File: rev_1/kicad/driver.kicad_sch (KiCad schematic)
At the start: 85 parts, among them Q1 IRFZ44NPBF, Q2 IRFZ44NPBF, Q3 IRFZ44NPBF, Q4 IRFZ44NPBF, Q5 IRFZ44NPBF, Q6 IRFZ44NPBF, U1 ir2104, U2 ir2104, U3 ir2104, U4 INA180A2IDBVR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

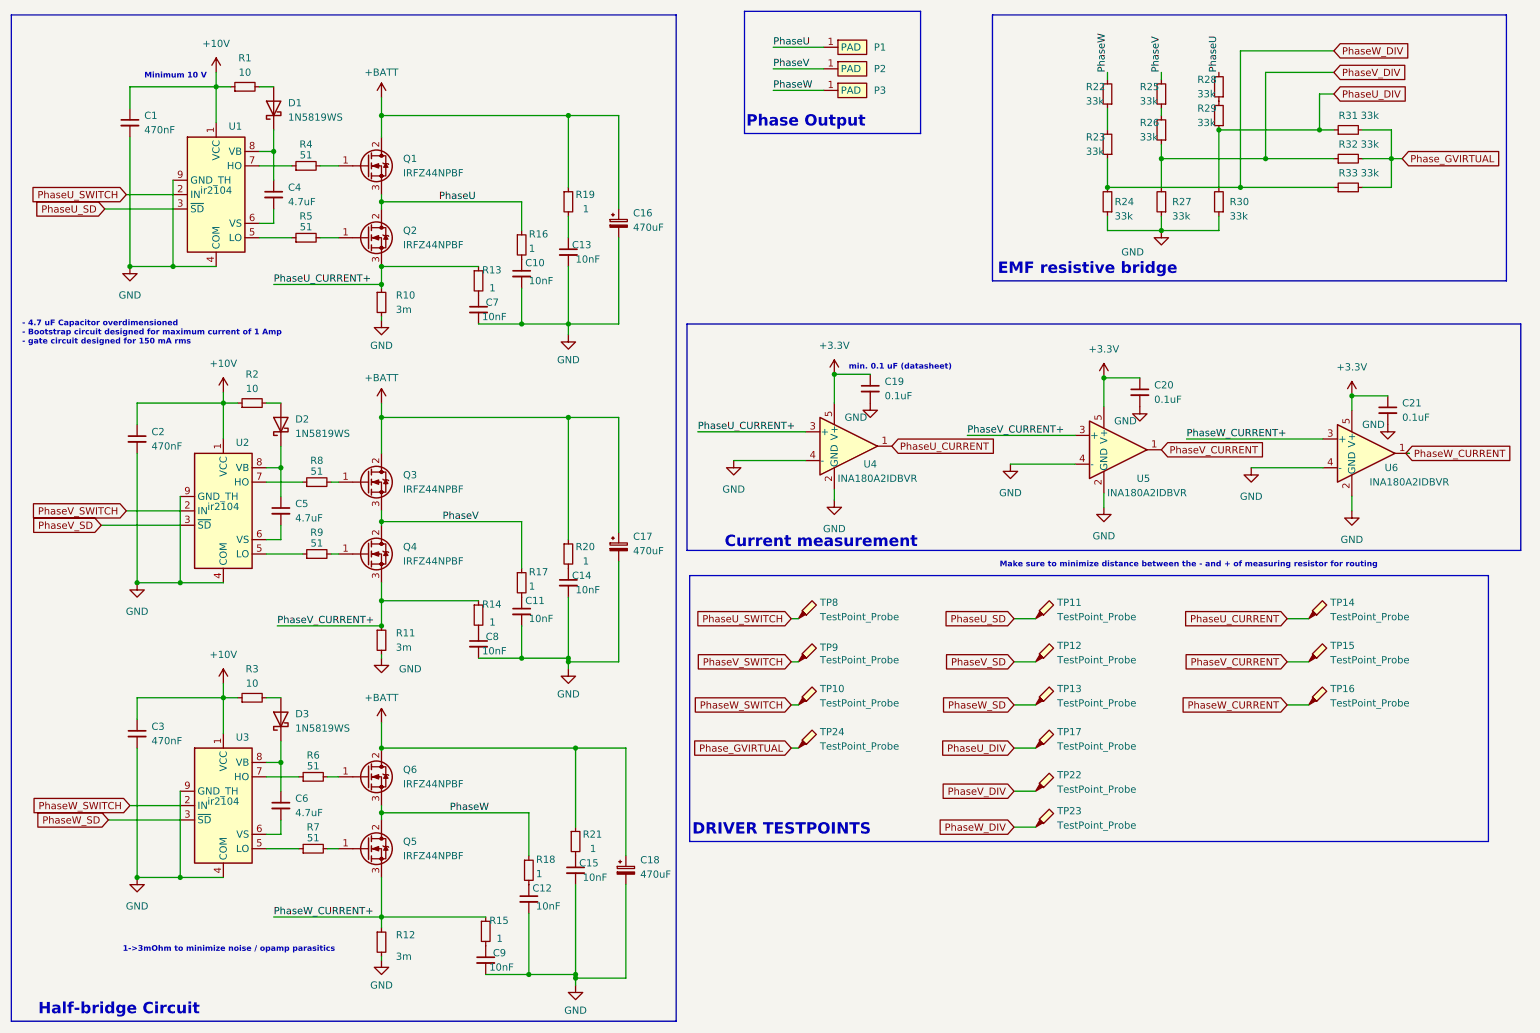
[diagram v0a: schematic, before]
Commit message: [kicad] (minor) Added comments about bldc strategy
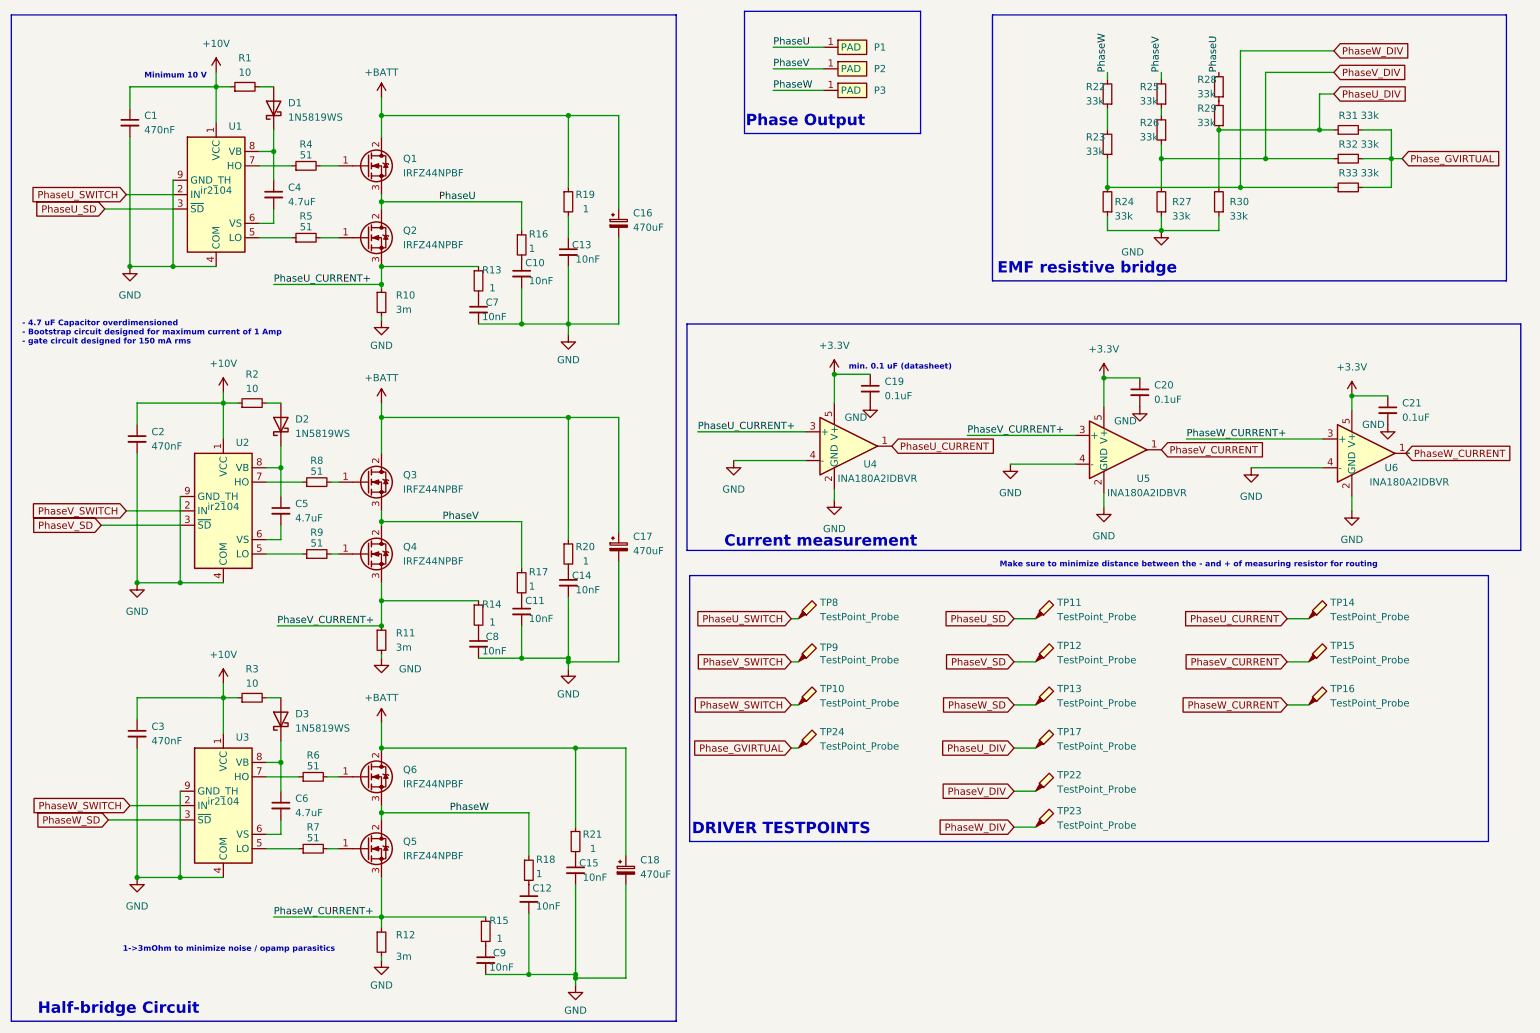
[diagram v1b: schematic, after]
